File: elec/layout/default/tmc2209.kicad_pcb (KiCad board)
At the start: 2 copper layers, 225.7 x 100.8 mm, 13 parts

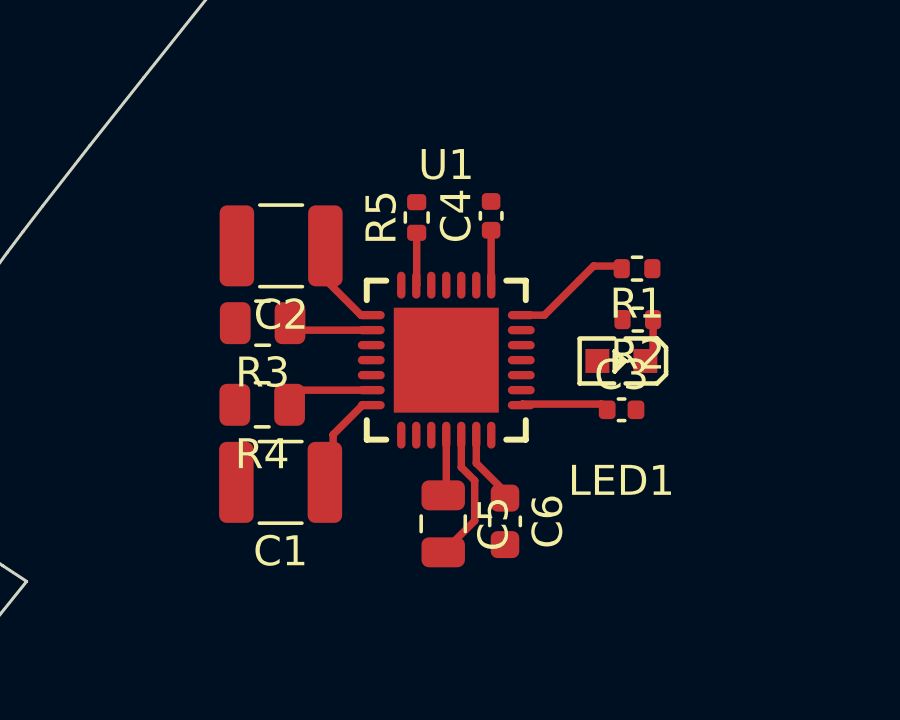
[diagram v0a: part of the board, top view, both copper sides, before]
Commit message: added enable button
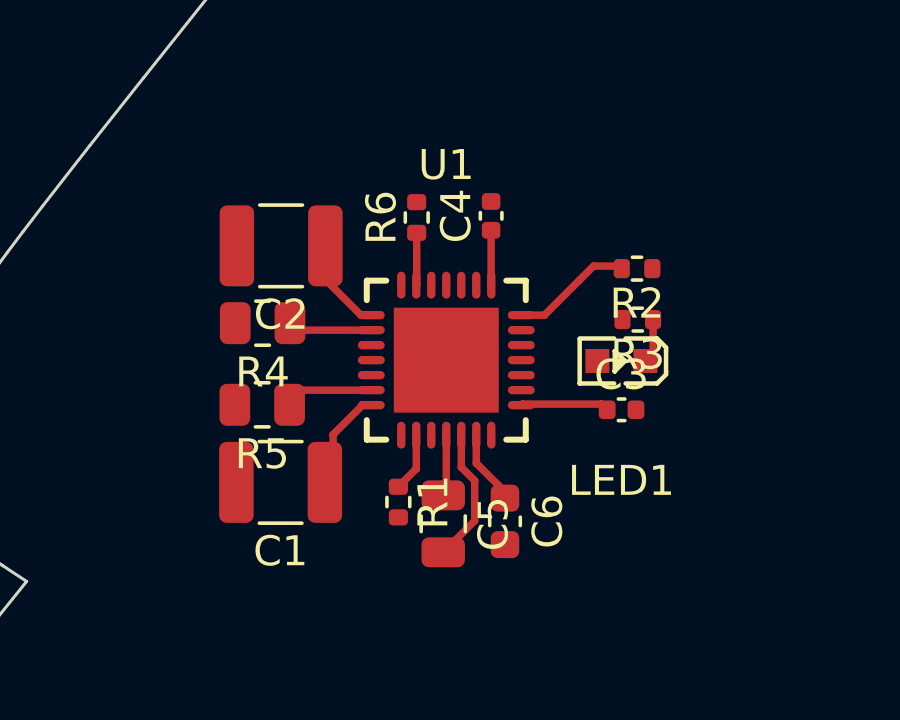
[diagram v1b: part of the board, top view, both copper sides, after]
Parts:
- added R1: Chip Resistor - Surface Mount 110KOhms ±5% 1/16W 0402 RoHS, lib:R0402, F.Cu at (151.5, 107.8)
- renumbered R1 to R2, R2 to R3, R3 to R4, R4 to R5, R5 to R6
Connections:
- U1 pad 7: spread -> gnd
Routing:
- net enn: track 0.00 -> 1.97 mm
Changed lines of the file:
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@@
   (net 20 "ms1_ad0")
   (net 21 "_5vout")
-  (net 22 "spread")
-  (net 23 "vcp")
-  (net 24 "cpi")
-  (net 25 "cpo")
-  (net 26 "enn")
-  (net 27 "ob2")
+  (net 22 "vcp")
+  (net 23 "cpi")
+  (net 24 "cpo")
+  (net 25 "enn")
+  (net 26 "ob2")
   (footprint "lib:QFN-28_L5.0-W5.0-P0.50-BL-EP" (layer "F.Cu")
     (at 153.145 103.075)
@@
       (stroke (width 0.06) (type solid)) (fill none) (layer "F.Fab"))
     (pad "1" smd oval (at -1.5 2.5 180) (size 0.28 0.9) (layers "F.Cu" "F.Paste" "F.Mask")
-      (net 27 "ob2") (pintype "stereo"))
+      (net 26 "ob2") (pintype "stereo"))
     (pad "2" smd oval (at -1 2.5 180) (size 0.28 0.9) (layers "F.Cu" "F.Paste" "F.Mask")
-      (net 26 "enn") (pintype "stereo"))
+      (net 25 "enn") (pintype "stereo"))
     (pad "3" smd oval (at -0.5 2.5 180) (size 0.28 0.9) (layers "F.Cu" "F.Paste" "F.Mask")
       (net 2 "gnd") (pintype "stereo"))
     (pad "4" smd oval (at 0 2.5 180) (size 0.28 0.9) (layers "F.Cu" "F.Paste" "F.Mask")
-      (net 25 "cpo") (pintype "stereo"))
+      (net 24 "cpo") (pintype "stereo"))
     (pad "5" smd oval (at 0.5 2.5 180) (size 0.28 0.9) (layers "F.Cu" "F.Paste" "F.Mask")
-      (net 24 "cpi") (pintype "stereo"))
+      (net 23 "cpi") (pintype "stereo"))
     (pad "6" smd oval (at 1 2.5 180) (size 0.28 0.9) (layers "F.Cu" "F.Paste" "F.Mask")
-      (net 23 "vcp") (pintype "stereo"))
+      (net 22 "vcp") (pintype "stereo"))
     (pad "7" smd oval (at 1.5 2.5 180) (size 0.28 0.9) (layers "F.Cu" "F.Paste" "F.Mask")
-      (net 22 "spread") (pintype "stereo"))
+      (net 2 "gnd") (pintype "stereo"))
     (pad "8" smd oval (at 2.5 1.5 90) (size 0.28 0.9) (layers "F.Cu" "F.Paste" "F.Mask")
       (net 21 "_5vout") (pintype "stereo"))
@@
     (tags "resistor")
     (attr smd)
-    (fp_text reference "R4" (at 0 -1.65 180) (layer "F.SilkS")
+    (fp_text reference "R5" (at 0 -1.65 180) (layer "F.SilkS")
         (effects (font (size 1 1) (thickness 0.15)))
     )
@@
     (tags "resistor")
     (attr smd)
-    (fp_text reference "R2" (at 0 -1.17 180) (layer "F.SilkS")
+    (fp_text reference "R3" (at 0 -1.17 180) (layer "F.SilkS")
         (effects (font (size 1 1) (thickness 0.15)))
     )
@@
     (tags "resistor")
     (attr smd)
-    (fp_text reference "R5" (at 0 -1.17 90) (layer "F.SilkS")
+    (fp_text reference "R6" (at 0 -1.17 90) (layer "F.SilkS")
         (effects (font (size 1 1) (thickness 0.15)))
     )
@@
       (stroke (width 0.1) (type solid)) (layer "F.Fab"))
     (pad "1" smd roundrect (at -0.95 0 270) (size 1 1.45) (layers "F.Cu" "F.Paste" "F.Mask") (roundrect_rratio 0.25)
-      (net 25 "cpo") (pintype "stereo"))
+      (net 24 "cpo") (pintype "stereo"))
     (pad "2" smd roundrect (at 0.95 0 270) (size 1 1.45) (layers "F.Cu" "F.Paste" "F.Mask") (roundrect_rratio 0.25)
-      (net 24 "cpi") (pintype "stereo"))
+      (net 23 "cpi") (pintype "stereo"))
     (model "${KICAD6_3DMODEL_DIR}/Capacitor_SMD.3dshapes/C_0805_2012Metric.wrl"
       (offset (xyz 0 0 0))
@@
     (tags "resistor")
     (attr smd)
-    (fp_text reference "R1" (at 0 -1.17 180) (layer "F.SilkS")
+    (fp_text reference "R2" (at 0 -1.17 180) (layer "F.SilkS")
         (effects (font (size 1 1) (thickness 0.15)))
     )
@@
     )
   )
+  (footprint "lib:R0402" (layer "F.Cu")
+    (at 151.547685 107.804841 -90)
+    (descr "Resistor SMD 0402 (1005 Metric), square (rectangular) end terminal, IPC_7351 nominal, (Body size source: IPC-SM-782 page 72, https://www.pcb-3d.com/wordpress/wp-content/uploads/ipc-sm-782a_amendment_1_and_2.pdf), generated with kicad-footprint-generator")
+    (tags "resistor")
+    (attr smd)
+    (fp_text reference "R1" (at 0 -1.17 90) (layer "F.SilkS")
+        (effects (font (size 1 1) (thickness 0.15)))
+    )
+    (fp_text value "Chip Resistor - Surface Mount 110KOhms ±5% 1/16W 0402 RoHS" (at 0 1.17 90) (layer "F.Fab")
+        (effects (font (size 1 1) (thickness 0.15)))
+    )
+    (fp_text user "${REFERENCE}" (at 0 0 90) (layer "F.Fab")
+        (effects (font (size 0.26 0.26) (thickness 0.04)))
+    )
+    (fp_line (start -0.153641 -0.38) (end 0.153641 -0.38)
+      (stroke (width 0.12) (type solid)) (layer "F.SilkS"))
+    (fp_line (start -0.153641 0.38) (end 0.153641 0.38)
+      (stroke (width 0.12) (type solid)) (layer "F.SilkS"))
+    (fp_line (start -0.93 -0.47) (end 0.93 -0.47)
+      (stroke (width 0.05) (type solid)) (layer "F.CrtYd"))
+    (fp_line (start -0.93 0.47) (end -0.93 -0.47)
+      (stroke (width 0.05) (type solid)) (layer "F.CrtYd"))
+    (fp_line (start 0.93 -0.47) (end 0.93 0.47)
+      (stroke (width 0.05) (type solid)) (layer "F.CrtYd"))
+    (fp_line (start 0.93 0.47) (end -0.93 0.47)
+      (stroke (width 0.05) (type solid)) (layer "F.CrtYd"))
+    (fp_line (start -0.525 -0.27) (end 0.525 -0.27)
+      (stroke (width 0.1) (type solid)) (layer "F.Fab"))
+    (fp_line (start -0.525 0.27) (end -0.525 -0.27)
+      (stroke (width 0.1) (type solid)) (layer "F.Fab"))
+    (fp_line (start 0.525 -0.27) (end 0.525 0.27)
+      (stroke (width 0.1) (type solid)) (layer "F.Fab"))
+    (fp_line (start 0.525 0.27) (end -0.525 0.27)
+      (stroke (width 0.1) (type solid)) (layer "F.Fab"))
+    (pad "1" smd roundrect (at -0.51 0 270) (size 0.54 0.64) (layers "F.Cu" "F.Paste" "F.Mask") (roundrect_rratio 0.25)
+      (net 25 "enn") (pintype "stereo"))
+    (pad "2" smd roundrect (at 0.51 0 270) (size 0.54 0.64) (layers "F.Cu" "F.Paste" "F.Mask") (roundrect_rratio 0.25)
+      (net 2 "gnd") (pintype "stereo"))
+    (model "${KICAD6_3DMODEL_DIR}/Resistor_SMD.3dshapes/R_0402_1005Metric.wrl"
+      (offset (xyz 0 0 0))
+      (scale (xyz 1 1 1))
+      (rotate (xyz 0 0 0))
+    )
+  )
   (footprint "lib:R0805" (layer "F.Cu")
     (at 147.023311 101.841571 180)
@@
     (tags "resistor")
     (attr smd)
-    (fp_text reference "R3" (at 0 -1.65 180) (layer "F.SilkS")
+    (fp_text reference "R4" (at 0 -1.65 180) (layer "F.SilkS")
         (effects (font (size 1 1) (thickness 0.15)))
     )
@@
       (stroke (width 0.1) (type solid)) (layer "F.Fab"))
     (pad "1" smd roundrect (at -0.775 0 270) (size 0.9 0.95) (layers "F.Cu" "F.Paste" "F.Mask") (roundrect_rratio 0.25)
-      (net 23 "vcp") (pintype "stereo"))
+      (net 22 "vcp") (pintype "stereo"))
     (pad "2" smd roundrect (at 0.775 0 270) (size 0.9 0.95) (layers "F.Cu" "F.Paste" "F.Mask") (roundrect_rratio 0.25)
       (net 6 "vcc") (pintype "stereo"))
@@
   (segment (start 155.68 104.54) (end 155.645 104.575) (width 0.25) (layer "F.Cu") (net 21))
   (segment (start 158.508629 104.729569) (end 158.31906 104.54) (width 0.25) (layer "F.Cu") (net 21))
-  (segment (start 154.145 106.507872) (end 154.145 105.575) (width 0.25) (layer "F.Cu") (net 23))
-  (segment (start 155.102401 107.673273) (end 155.102401 107.465273) (width 0.25) (layer "F.Cu") (net 23))
-  (segment (start 155.102401 107.465273) (end 154.145 106.507872) (width 0.25) (layer "F.Cu") (net 23))
-  (segment (start 153.645 106.644268) (end 154.092833 107.092101) (width 0.25) (layer "F.Cu") (net 24))
-  (segment (start 153.645 105.575) (end 153.645 106.644268) (width 0.25) (layer "F.Cu") (net 24))
-  (segment (start 154.092833 107.092101) (end 154.092833 108.430274) (width 0.25) (layer "F.Cu") (net 24))
-  (segment (start 154.092833 108.430274) (end 153.042833 109.480274) (width 0.25) (layer "F.Cu") (net 24))
-  (segment (start 153.145 105.575) (end 153.145 107.478107) (width 0.25) (layer "F.Cu") (net 25))
-  (segment (start 153.145 107.478107) (end 153.042833 107.580274) (width 0.25) (layer "F.Cu") (net 25))
+  (segment (start 154.145 106.507872) (end 154.145 105.575) (width 0.25) (layer "F.Cu") (net 22))
+  (segment (start 155.102401 107.673273) (end 155.102401 107.465273) (width 0.25) (layer "F.Cu") (net 22))
+  (segment (start 155.102401 107.465273) (end 154.145 106.507872) (width 0.25) (layer "F.Cu") (net 22))
+  (segment (start 153.645 106.644268) (end 154.092833 107.092101) (width 0.25) (layer "F.Cu") (net 23))
+  (segment (start 153.645 105.575) (end 153.645 106.644268) (width 0.25) (layer "F.Cu") (net 23))
+  (segment (start 154.092833 107.092101) (end 154.092833 108.430274) (width 0.25) (layer "F.Cu") (net 23))
+  (segment (start 154.092833 108.430274) (end 153.042833 109.480274) (width 0.25) (layer "F.Cu") (net 23))
+  (segment (start 153.145 105.575) (end 153.145 107.478107) (width 0.25) (layer "F.Cu") (net 24))
+  (segment (start 153.145 107.478107) (end 153.042833 107.580274) (width 0.25) (layer "F.Cu") (net 24))
+  (segment (start 152.145 106.697526) (end 152.145 105.575) (width 0.25) (layer "F.Cu") (net 25))
+  (segment (start 151.547685 107.294841) (end 152.145 106.697526) (width 0.25) (layer "F.Cu") (net 25))
   (group "" (id 6c1ef9f7-0f34-47bb-ac1a-76df23fb396e)
     (members
